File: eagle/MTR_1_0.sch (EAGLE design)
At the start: 27 parts, among them IC1 L298, X1 In A, X2 In B

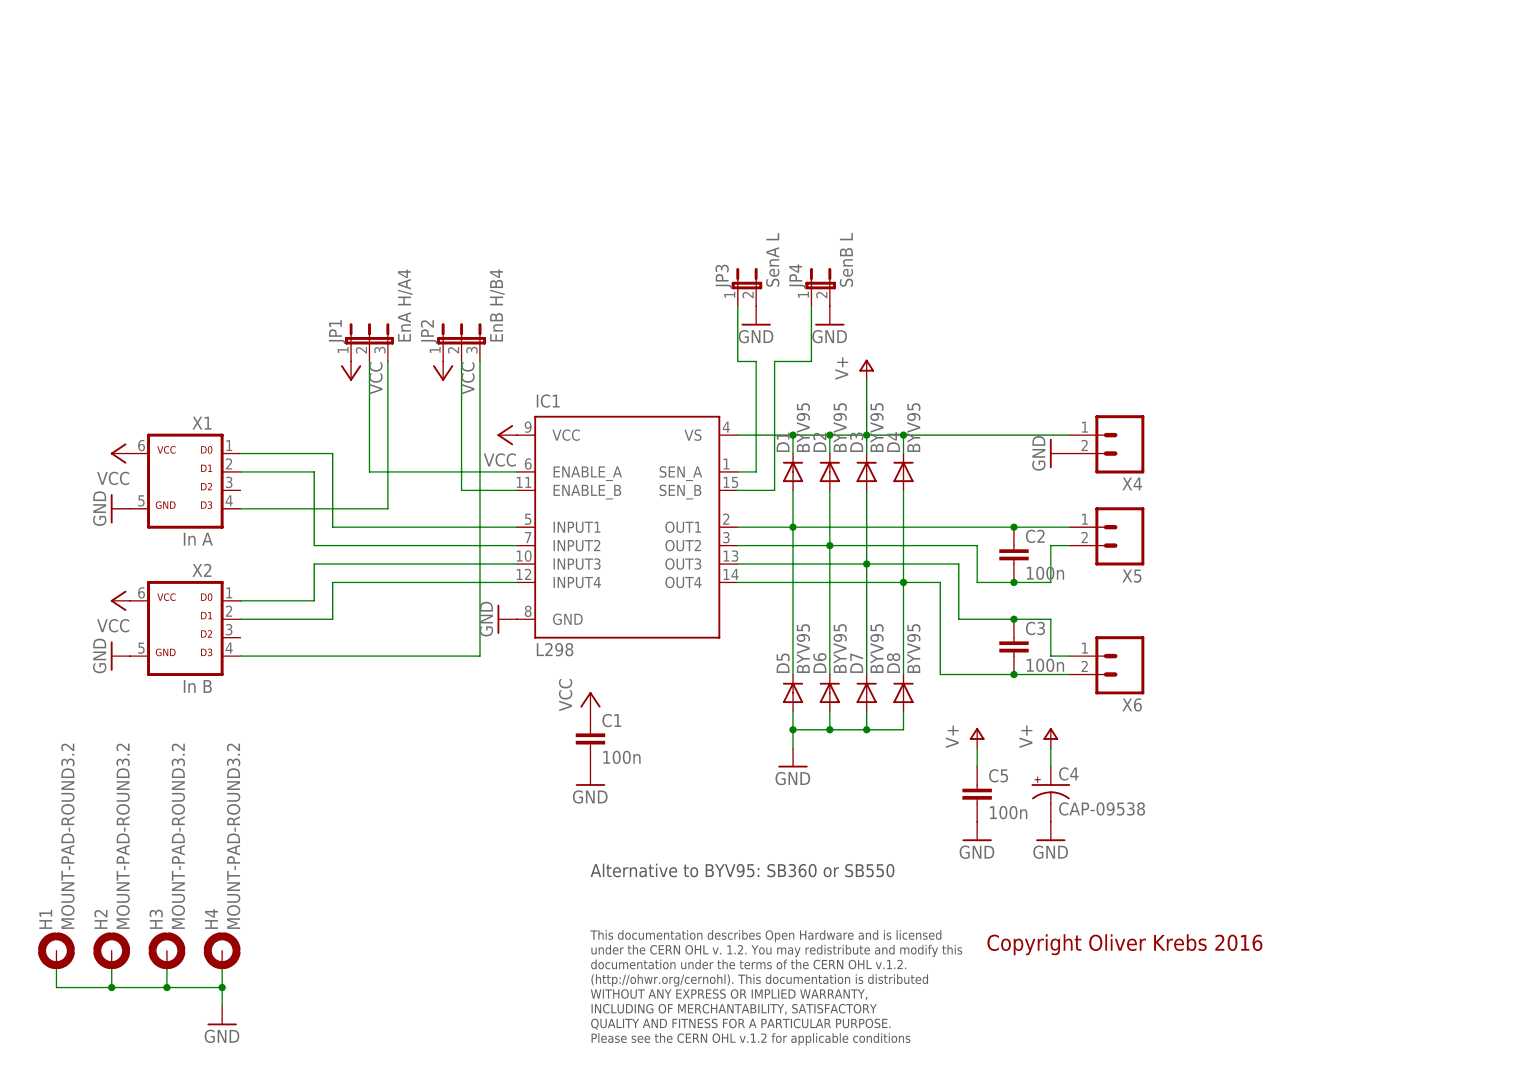
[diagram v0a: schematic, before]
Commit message: Add new tetra-Board and arduino files
Add AMP_1_0, AVC_1_0, D18_1_1, IOP_1_2, MIC_1_0, PIN_1_1, POT_1_0, PWA_1_0, PWR_1_0, RGF 2.0, SOC_2_0, VLT_1_0
Add mex_nano_shield_keyboard, mex_nano_shied_numbers

New arduino projects
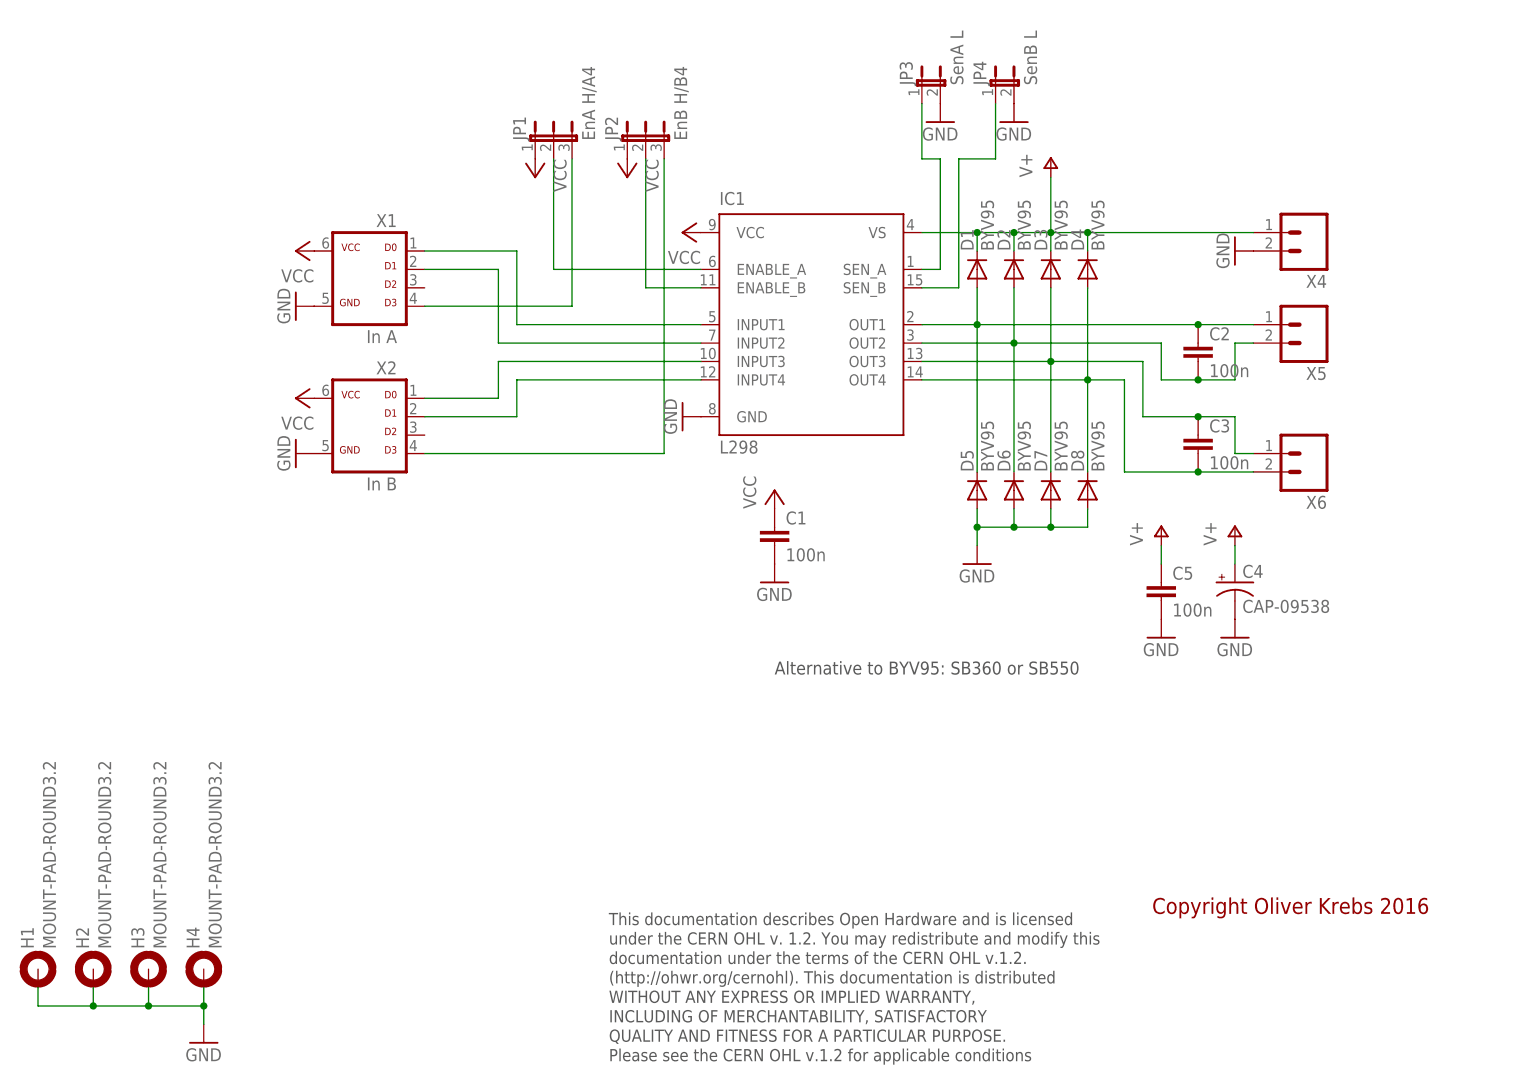
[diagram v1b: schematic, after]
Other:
- moved on the sheet: C1, C2, C3, C4, C5, D1, D2, D3, D4, D5, D6, D7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
